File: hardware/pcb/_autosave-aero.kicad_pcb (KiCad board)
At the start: 4 copper layers, 39.1 x 46.2 mm, 90 parts, among them CON1 USB-MICRO-B, CON2 MMCX_CONN, J1 CORTEX_DBG_CONN, J2 LiPoly_Conn, Q1 Q_NPN_BEC, SW1 SW_PUSH, U1 STM32L151C8, U2 nRF8001, U3 ms5611, U4 BMX055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

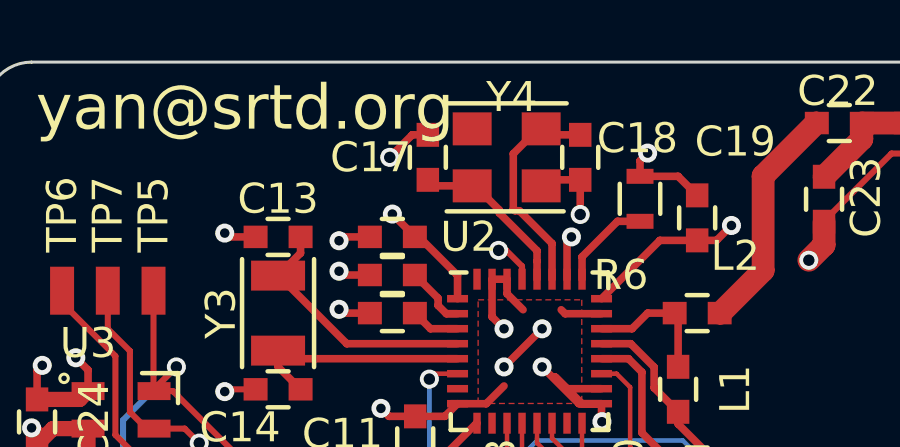
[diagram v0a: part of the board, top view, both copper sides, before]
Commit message: fixed a few known pcb issues
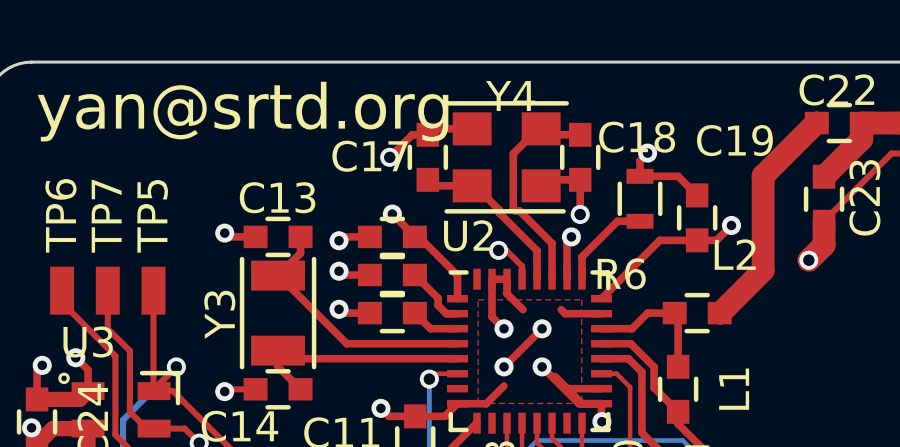
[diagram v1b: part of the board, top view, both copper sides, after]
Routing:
- net GND: track 173.3 -> 174.8 mm
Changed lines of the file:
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@@
   (general
     (links 228)
-    (no_connects 10)
+    (no_connects 2)
     (area 130.175 79.375 249.555001 164.244001)
     (thickness 1.6)
     (drawings 12)
-    (tracks 1069)
+    (tracks 1071)
     (zones 0)
     (modules 90)
@@
   )
   (setup
-    (last_trace_width 0.254)
+    (last_trace_width 0.1524)
     (user_trace_width 0.1524)
     (user_trace_width 0.2032)
@@
   (via (at 165.7992 143.51) (size 0.635) (layers F.Cu B.Cu) (net 2))
   (segment (start 179.238069 115.797389) (end 179.038069 115.997389) (width 0.254) (layer F.Cu) (net 2))
+  (segment (start 175.46 113.985) (end 175.26 114.185) (width 0.254) (layer F.Cu) (net 2))
+  (segment (start 176.738069 113.985) (end 175.46 113.985) (width 0.254) (layer F.Cu) (net 2))
   (segment (start 188.1077 137.3705) (end 187.4527 136.7155) (width 0.254) (layer F.Cu) (net 3))
   (segment (start 189.2427 137.3705) (end 188.1077 137.3705) (width 0.254) (layer F.Cu) (net 3))
